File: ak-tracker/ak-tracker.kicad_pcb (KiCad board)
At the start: 2 copper layers, 30.5 x 48.3 mm, 13 parts, among them J1 left, J2 right, SW2 Reset, SW3 SW_DIP_x02, U1 BMA400, U2 TPL5010

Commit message: better routing
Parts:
- WD Acc: renamed from SW3
- moved R2 5.70 mm to (55.9, 70.1), turned to 90 degrees
- moved C1 4.07 mm to (59.5, 70.6)
- moved U1 4.07 mm to (59.7, 67.3)
- moved R5 3.97 mm to (63.0, 67.3)
- moved R1 3.21 mm to (55.9, 65.0), turned to -90 degrees
- moved R4 2.57 mm to (68.6, 78.2)
- moved Reset 2.54 mm to (57.4, 79.9)
- moved U2 2.54 mm to (68.7, 82.2)
- moved WD Acc 2.54 mm to (68.6, 68.6)
- moved C2 2.31 mm to (64.0, 82.0)
- moved R3 1.85 mm to (68.6, 85.6)
- renumbered SW2 to Reset
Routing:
- net SDA: track 16.9 -> 9.42 mm
- net SCL: track 9.18 -> 16.0 mm
- net ~{RST}: track 17.5 -> 20.8 mm
- net WOKE: track 17.5 -> 20.1 mm
- net /VDD2: track 31.1 -> 28.8 mm
- net /VDD1: track 26.3 -> 24.1 mm
- net VCC: track 13.1 -> 14.7 mm
- net Net-(U1-VDDIO): track 12.2 -> 10.7 mm
- net MOVED: track 16.0 -> 17.4 mm
- net WAKE: track 16.9 -> 18.3 mm
- net GND: track 7.06 -> 7.40 mm, vias 8 -> 10
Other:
- outline, holes or cut-outs redrawn

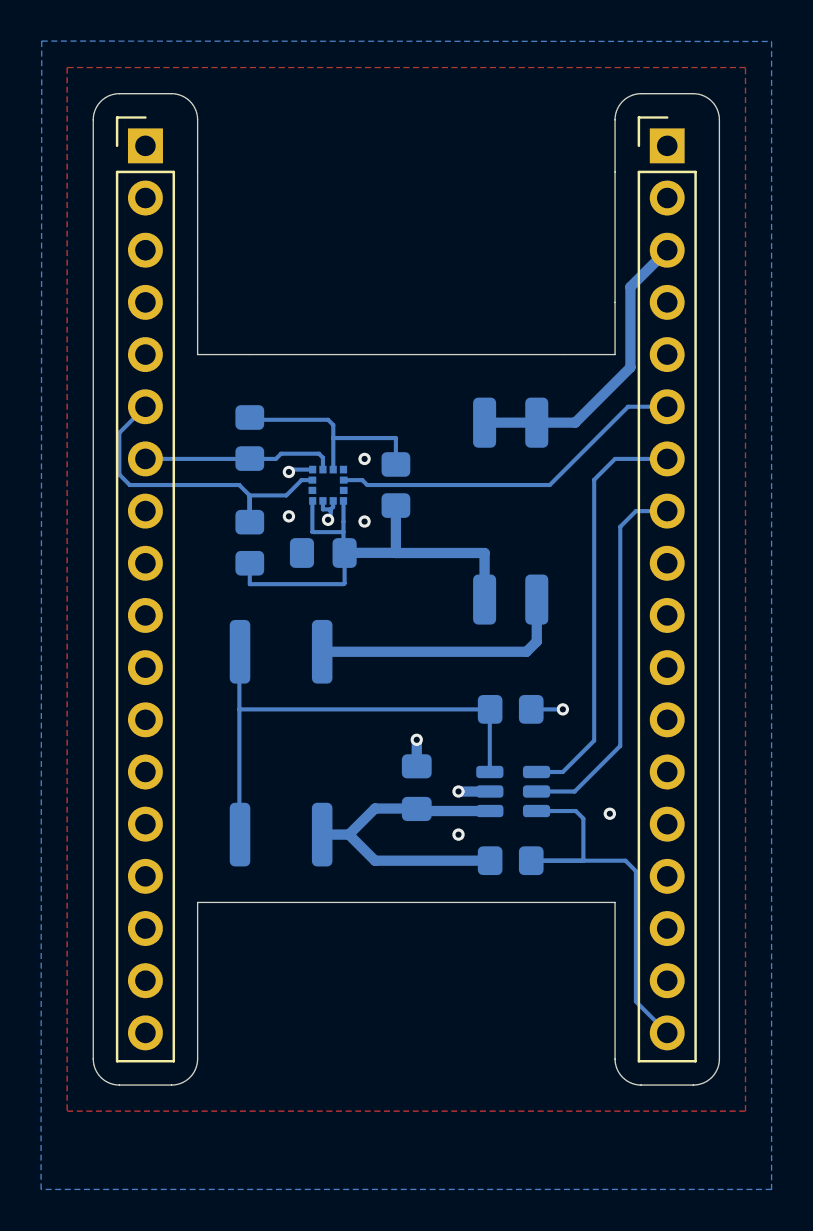
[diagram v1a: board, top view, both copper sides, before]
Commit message: interrupts to 5,6,7
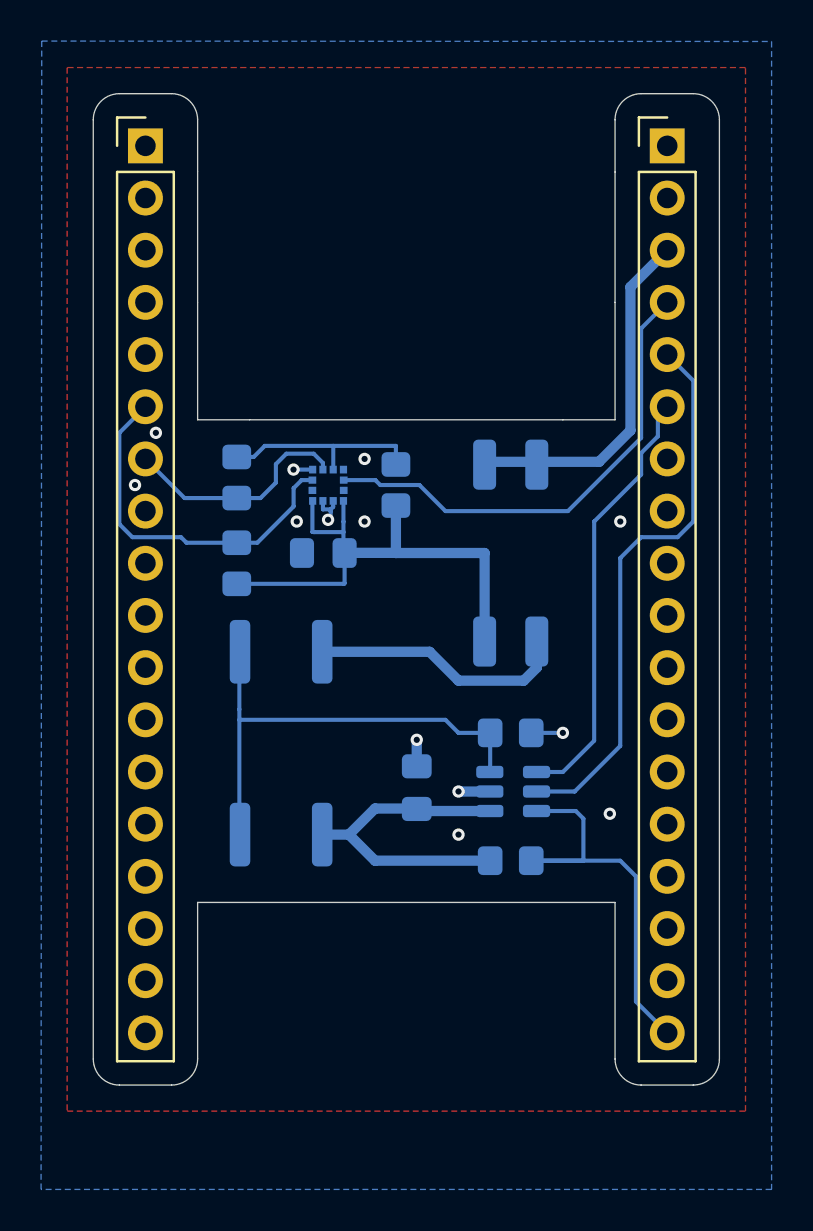
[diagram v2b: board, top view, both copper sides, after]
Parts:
- C1, C2: value C -> 100n
- SW3: renamed from WD Acc
- moved SW3 2.05 mm to (68.6, 70.6)
- moved R1 2.02 mm to (55.2, 66.9)
- moved R2 1.18 mm to (55.2, 71.1)
- moved R4 1.14 mm to (68.6, 79.4)
- renumbered Reset to SW2
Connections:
- J2 pad 4: unconnected-(J2-Pin_4-Pad4) -> MOVED
- J2 pad 5: unconnected-(J2-Pin_5-Pad5) -> WAKE
- J2 pad 6: MOVED -> WOKE
- J2 pad 7: WOKE -> unconnected-(J2-Pin_7-Pad7)
- J2 pad 8: WAKE -> unconnected-(J2-Pin_8-Pad8)
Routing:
- net WAKE: track 18.3 -> 27.1 mm
- net MOVED: track 17.4 -> 23.7 mm
- net VCC: track 14.7 -> 17.2 mm
- net SDA: track 9.42 -> 11.4 mm
- net SCL: track 16.0 -> 17.8 mm
- net /VDD1: track 24.1 -> 25.6 mm
- net WOKE: track 20.1 -> 21.2 mm
- net Net-(U2-DELAY/M_RST): track 24.2 -> 23.3 mm
- net Net-(U1-VDDIO): track 10.7 -> 10.0 mm
- net GND: track 7.40 -> 7.13 mm, vias 10 -> 13
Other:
- outline, holes or cut-outs redrawn

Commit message: 3k3 & silk screen
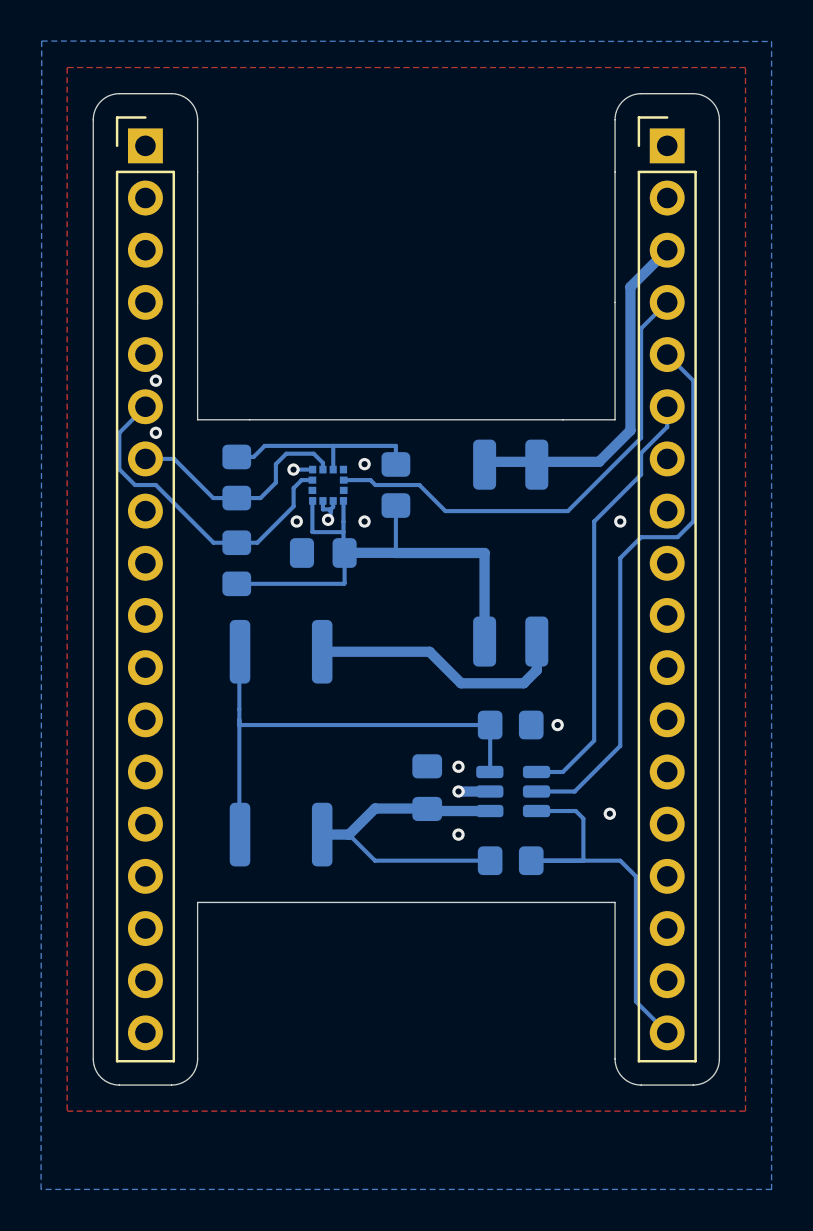
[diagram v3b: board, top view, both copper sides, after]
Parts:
- R1, R2: value 2k2 -> 3k3
- SW3: value SW_DIP_x02 -> Wd Acc
- moved C2 0.51 mm to (64.5, 82.0)
- moved R4 0.38 mm to (68.6, 79.0)
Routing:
- net GND: track 7.13 -> 4.73 mm
- net SCL: track 17.8 -> 16.2 mm
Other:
- board text added: "gnd vcc mv wa wo"
- board text added: "gnd vxt"
- board text added: "rst"
- board text added: "scl sda"
